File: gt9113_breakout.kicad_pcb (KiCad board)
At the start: 4 copper layers, 34.8 x 36 mm, 53 parts, among them J1 Conn_01x04_Male, J2 CONN_10118194-0001LF_AMP, J3 Conn_01x04_Male, J4 Conn_01x07_Male, J5 Conn_01x01_Male, J7 504740-5100, J8 504740-5100, Q1 2N7002E, U1 mXT2952TD, U2 HT7533-1-SOT89, Y1 DNF/16MHz

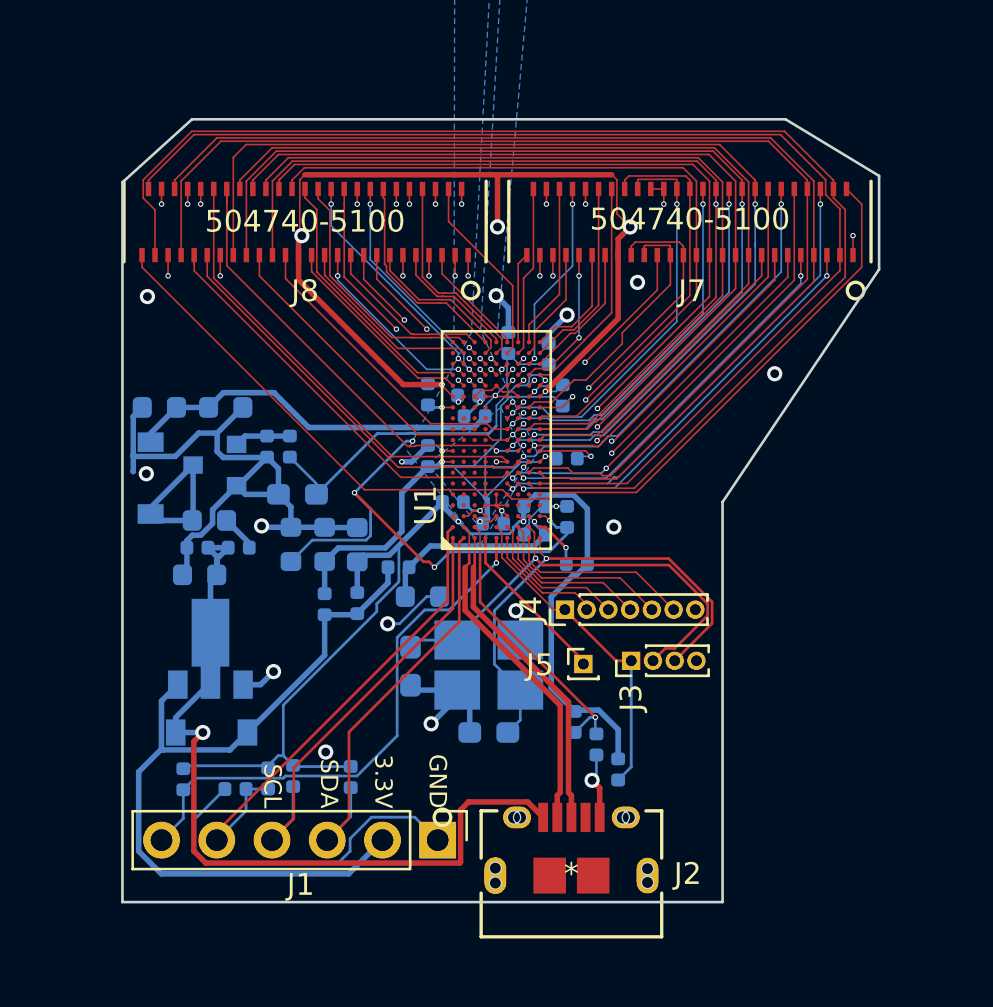
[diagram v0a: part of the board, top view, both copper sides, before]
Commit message: Remove all traces of atmxt2952. enable pth_and_npth_single_file since that's what jlcpcb wants
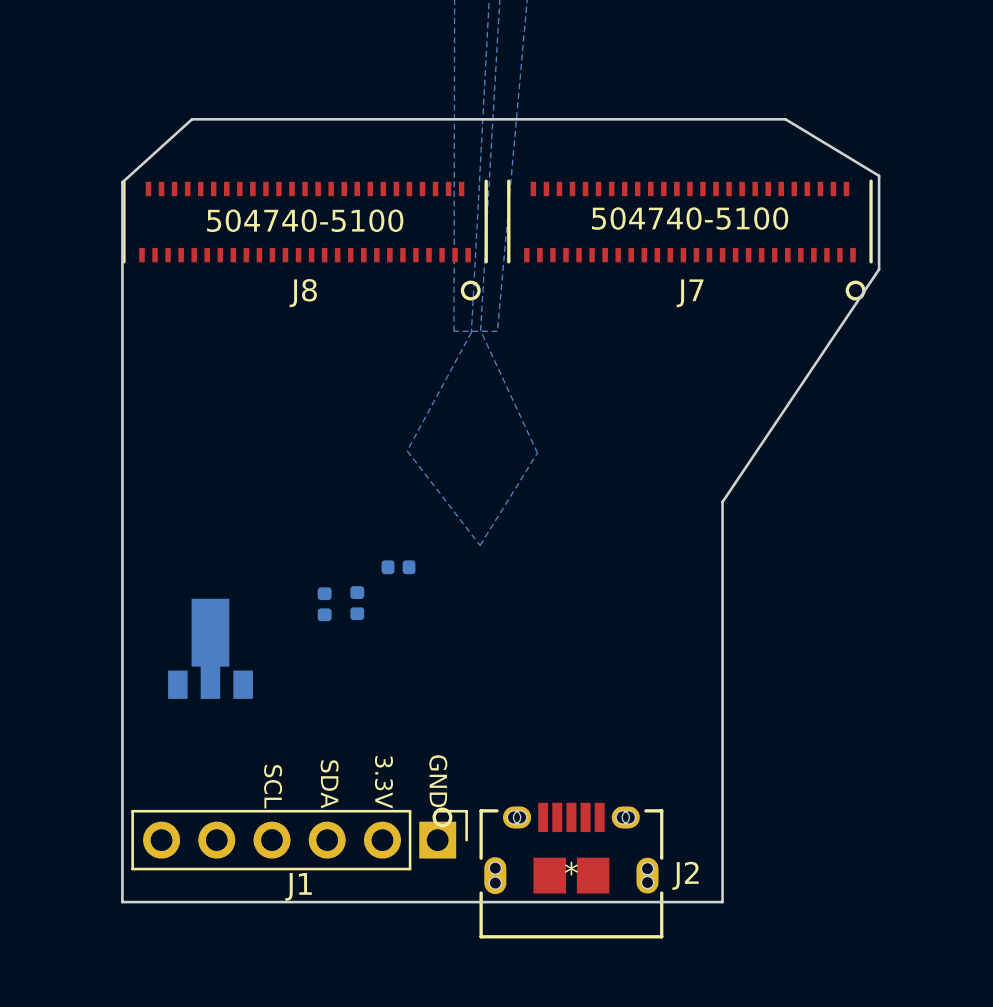
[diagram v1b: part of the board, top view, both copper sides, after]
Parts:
- removed C1, C11, C18, C20, C23, C7: 2.2uF, Capacitor_SMD:C_0603_1608Metric
- removed C10, C12, C13, C14, C16, C17, C19, C2, C21, C22, C25, C26, C8, C9: 22nF, Capacitor_SMD:C_0402_1005Metric
- removed C24, C27: DNF/15pF, Capacitor_SMD:C_0603_1608Metric_Pad1.05x0.95mm_HandSolder
- removed C3: DNF/33pF, Capacitor_SMD:C_0603_1608Metric_Pad1.05x0.95mm_HandSolder
- removed C4: 33pF, Capacitor_SMD:C_0402_1005Metric
- removed C5: 10nF, Capacitor_SMD:C_0402_1005Metric
- removed C6: 10uF, Capacitor_SMD:C_0603_1608Metric
- removed D1, D2: D_Schottky, Diode_SMD:D_SOD-123
- removed J3: Conn_01x04_Male, Connector_PinHeader_1.00mm:PinHeader_1x04_P1.00mm_Vertical
- removed J4: Conn_01x07_Male, Connector_PinHeader_1.00mm:PinHeader_1x07_P1.00mm_Vertical
- removed J5: Conn_01x01_Male, Connector_PinHeader_1.00mm:PinHeader_1x01_P1.00mm_Vertical
- removed L1: 10uH, Inductor_SMD:L_0603_1608Metric
- removed Q1: 2N7002E, Package_TO_SOT_SMD:SOT-23
- removed R1: 10, Resistor_SMD:R_0402_1005Metric
- removed R13, R3, R4: 10k, Resistor_SMD:R_0402_1005Metric
- removed R2: 47, Resistor_SMD:R_0402_1005Metric
- removed R5: 47k, Resistor_SMD:R_0402_1005Metric
- removed R6, R7: 3.3k, Resistor_SMD:R_0402_1005Metric
- removed R8: 0, Resistor_SMD:R_0402_1005Metric
- removed R9: 100k, Resistor_SMD:R_0402_1005Metric
- removed U1: mXT2952TD, mXT2952TD:mXT2952TD
- removed Y1: DNF/16MHz, Crystal:Crystal_SMD_3225-4Pin_3.2x2.5mm_HandSoldering
- J2: value CONN_10118194-0001LF_AMP -> 10118194-0001LF
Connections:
- net /VBUS renamed /VIN_5.0
- J1 pad 3: /SDA -> (no net)
- J1 pad 4: /SCL -> (no net)
- J1 pad 5: /~RESET -> (no net)
- J1 pad 6: /~CHG -> (no net)
- J2 pad 2: /USBD- -> (no net)
- J2 pad 3: /USBD+ -> (no net)
- J2 pad 4: Net-(J2-Pad4) -> (no net)
- J7 pad 31: /Y29 -> (no net)
- J7 pad 38: /X0 -> (no net)
- J7 pad 39: /X1 -> (no net)
- J7 pad 40: /X2 -> (no net)
- J7 pad 41: /X3 -> (no net)
- J7 pad 42: /X4 -> (no net)
- J7 pad 43: /X5 -> (no net)
- J7 pad 44: /X6 -> (no net)
- J7 pad 45: /X7 -> (no net)
- J7 pad 46: /X8 -> (no net)
- J7 pad 47: /X9 -> (no net)
- J7 pad 48: /X10 -> (no net)
- J7 pad 49: /X11 -> (no net)
- J7 pad 50: /X12 -> (no net)
- J7 pad 51: /X13 -> (no net)
- J8 pad 1: /X14 -> (no net)
- J8 pad 10: /X23 -> (no net)
- J8 pad 11: /X24 -> (no net)
- J8 pad 12: /X25 -> (no net)
- J8 pad 13: /X26 -> (no net)
- J8 pad 14: /X27 -> (no net)
- J8 pad 15: /X28 -> (no net)
- J8 pad 16: /X29 -> (no net)
- J8 pad 17: /X30 -> (no net)
- J8 pad 18: /X31 -> (no net)
- J8 pad 19: /X32 -> (no net)
- J8 pad 2: /X15 -> (no net)
- J8 pad 20: /X33 -> (no net)
- J8 pad 21: /X34 -> (no net)
- J8 pad 22: /X35 -> (no net)
- J8 pad 23: /X36 -> (no net)
- J8 pad 24: /X37 -> (no net)
- J8 pad 25: /X38 -> (no net)
- J8 pad 26: /X39 -> (no net)
- J8 pad 3: /X16 -> (no net)
- J8 pad 4: /X17 -> (no net)
- J8 pad 5: /X18 -> (no net)
- J8 pad 6: /X19 -> (no net)
- J8 pad 7: /X20 -> (no net)
- J8 pad 8: /X21 -> (no net)
- J8 pad 9: /X22 -> (no net)
- R11 pad 1: /VDDIO -> (no net)
- R12 pad 1: /VDD -> (no net)
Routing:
- net GND: track 132.0 -> 0.00 mm, vias 27 -> 0
- net /Y2: track 60.6 -> 0.00 mm
- net /Y1: track 55.6 -> 0.00 mm
- net /Y6: track 55.0 -> 0.00 mm
- net /Y5: track 52.5 -> 0.00 mm
- net /VDDIO: track 50.6 -> 0.00 mm, vias 2 -> 0
- net /Y14: track 49.1 -> 0.00 mm, vias 2 -> 0
- net /Y0: track 46.4 -> 0.00 mm
- net /Y16: track 45.1 -> 0.00 mm, vias 2 -> 0
- net /AVDD: track 44.8 -> 0.00 mm, vias 5 -> 0
- net /Y3: track 44.3 -> 0.00 mm, vias 3 -> 0
- net /Y4: track 43.5 -> 0.00 mm, vias 3 -> 0
- net /Y15: track 42.5 -> 0.00 mm
- net /Y17: track 41.4 -> 0.00 mm, vias 2 -> 0
- net /Y7: track 41.2 -> 0.00 mm, vias 3 -> 0
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- removed copper zone on B.Cu, net /AVDD
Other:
- net class BGA removed
- net class Default: clearance 0.0762 -> 0.127; trace_width 0.0762 -> 0.127; via_dia 0.25 -> 0.45; via_drill 0.15 -> 0.2
- rule trace_clearance: 0.0762 -> 0.127
- rule trace_min: 0.076 -> 0.127
- rule via_min_drill: 0.15 -> 0.2
- rule via_min_size: 0.25 -> 0.45

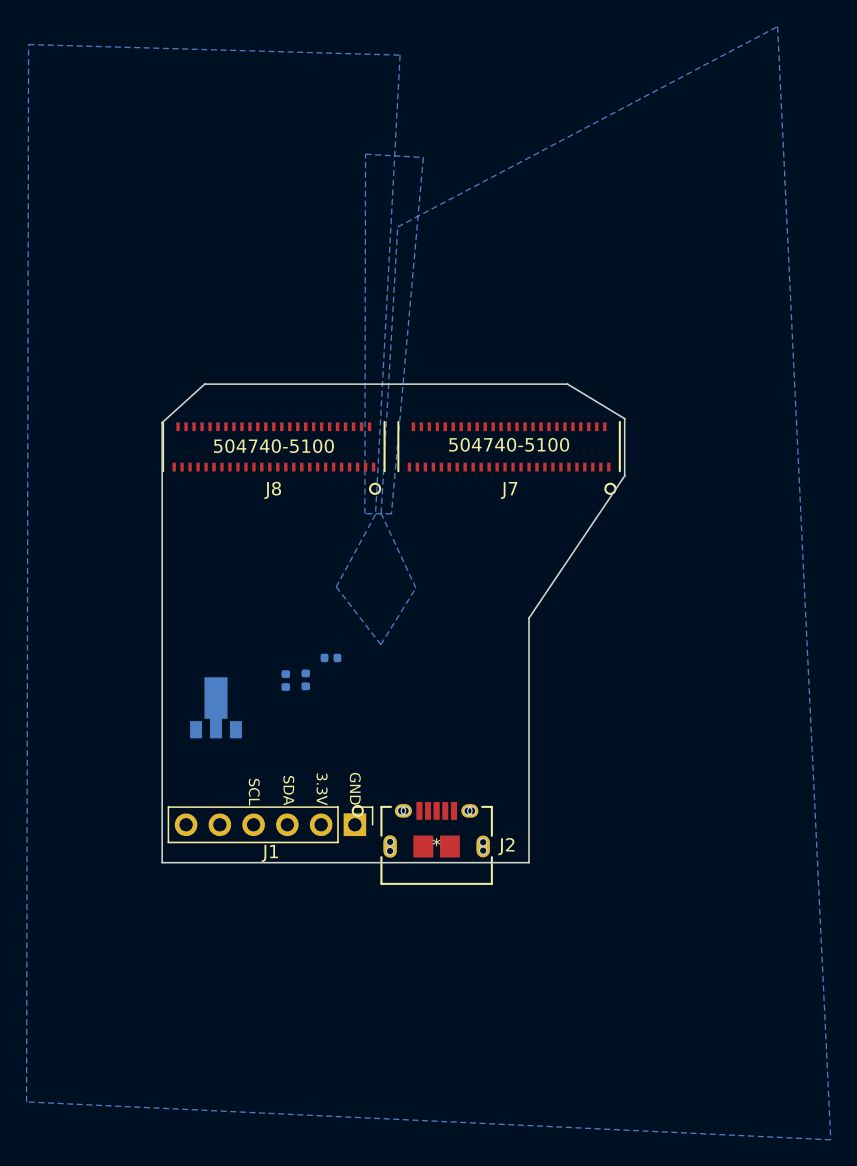
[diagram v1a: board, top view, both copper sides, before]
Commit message: Add footprint for GT9113. Start to route the drive/sense pins.
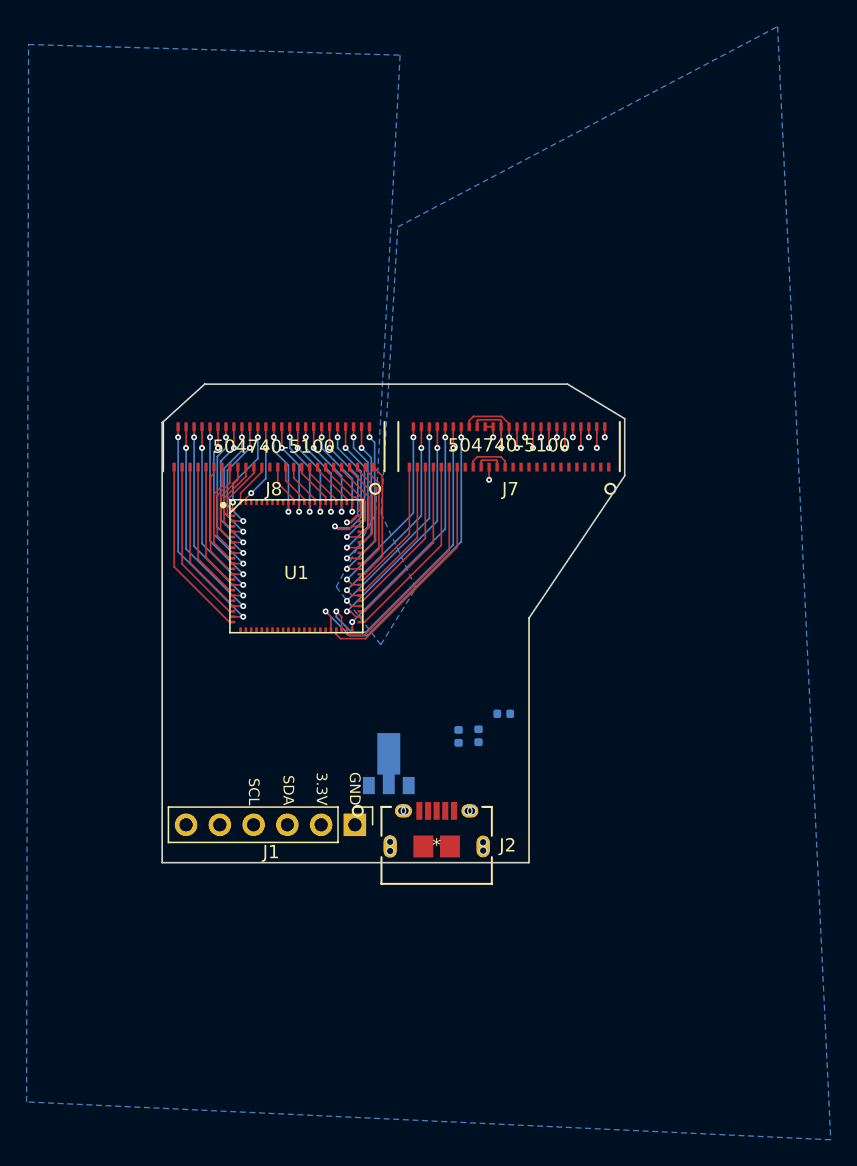
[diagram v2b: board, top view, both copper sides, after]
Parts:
- added U1: GT9113, footprints:GT9113, F.Cu at (138.9, 83.7)
- moved R10 13.7 mm to (151.1, 96.5)
- moved R11 13.7 mm to (152.6, 96.5)
- moved R12 13.7 mm to (154.5, 94.8)
- moved U2 13.7 mm to (145.8, 98.5)
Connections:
- J7 pad 31: (no net) -> /Y29
- J7 pad 38: (no net) -> /X0
- J7 pad 39: (no net) -> /X1
- J7 pad 40: (no net) -> /X2
- J7 pad 41: (no net) -> /X3
- J7 pad 42: (no net) -> /X4
- J7 pad 43: (no net) -> /X5
- J7 pad 44: (no net) -> /X6
- J7 pad 45: (no net) -> /X7
- J7 pad 46: (no net) -> /X8
- J7 pad 47: (no net) -> /X9
- J7 pad 48: (no net) -> /X10
- J7 pad 49: (no net) -> /X11
- J7 pad 50: (no net) -> /X12
- J7 pad 51: (no net) -> /X13
- J8 pad 1: (no net) -> /X14
- J8 pad 10: (no net) -> /X23
- J8 pad 11: (no net) -> /X24
- J8 pad 12: (no net) -> /X25
- J8 pad 13: (no net) -> /X26
- J8 pad 14: (no net) -> /X27
- J8 pad 15: (no net) -> /X28
- J8 pad 16: (no net) -> /X29
- J8 pad 17: (no net) -> /X30
- J8 pad 18: (no net) -> /X31
- J8 pad 19: (no net) -> /X32
- J8 pad 2: (no net) -> /X15
- J8 pad 20: (no net) -> /X33
- J8 pad 21: (no net) -> /X34
- J8 pad 22: (no net) -> /X35
- J8 pad 23: (no net) -> /X36
- J8 pad 24: (no net) -> /X37
- J8 pad 25: (no net) -> /X38
- J8 pad 26: (no net) -> /X39
- J8 pad 3: (no net) -> /X16
- J8 pad 4: (no net) -> /X17
- J8 pad 5: (no net) -> /X18
- J8 pad 6: (no net) -> /X19
- J8 pad 7: (no net) -> /X20
- J8 pad 8: (no net) -> /X21
- J8 pad 9: (no net) -> /X22
- R10 pad 1: /AVDD -> (no net)
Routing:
- net /X0: track 0.00 -> 24.1 mm, vias 0 -> 2
- net /X2: track 0.00 -> 22.9 mm, vias 0 -> 2
- net /X1: track 0.00 -> 18.4 mm
- net /X4: track 0.00 -> 18.2 mm, vias 0 -> 2
- net /X6: track 0.00 -> 17.9 mm, vias 0 -> 2
- net /Y1: track 0.00 -> 17.1 mm, vias 0 -> 2
- net /X3: track 0.00 -> 17.0 mm
- net /X8: track 0.00 -> 16.8 mm, vias 0 -> 2
- net /Y3: track 0.00 -> 16.1 mm, vias 0 -> 2
- net /X10: track 0.00 -> 15.8 mm, vias 0 -> 2
- net /Y5: track 0.00 -> 15.0 mm, vias 0 -> 2
- net /X12: track 0.00 -> 14.7 mm, vias 0 -> 2
- net /Y0: track 0.00 -> 14.4 mm, vias 0 -> 1
- net /X5: track 0.00 -> 14.4 mm
- net /Y2: track 0.00 -> 14.2 mm, vias 0 -> 1
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
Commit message: Fix up USB connector footprint so I don't have to ignore DRC errors. Add courtyard for gt9113 footprint. Wire up digital IO pins to 2.54mm header. Tweak X/Y traces.
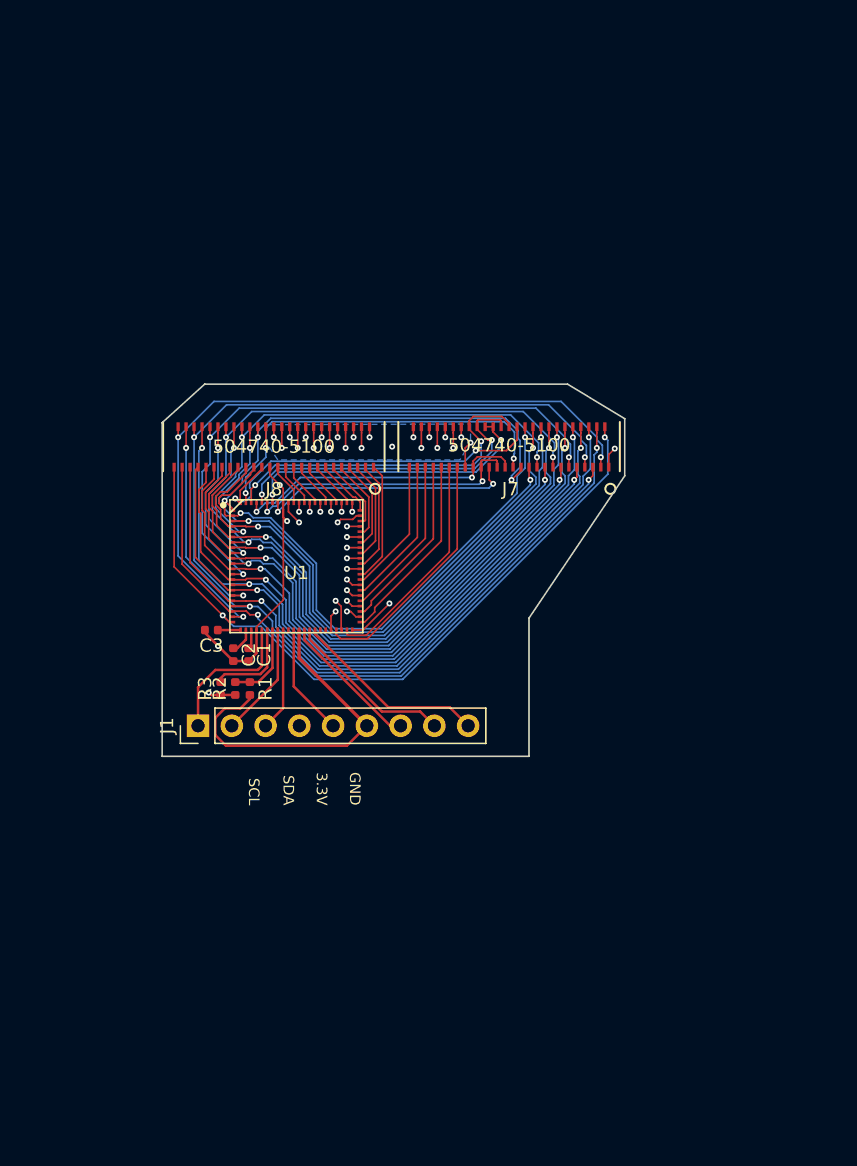
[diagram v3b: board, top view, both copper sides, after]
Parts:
- removed J2: 10118194-0001LF, usb port:10118194-0001LF
- removed R10, R11, R12: 0, Resistor_SMD:R_0402_1005Metric
- removed U2: HT7533-1-SOT89, Package_TO_SOT_SMD:SOT-89-3
- added C1: 2.2uF, Capacitor_SMD:C_0402_1005Metric, F.Cu at (135.3, 90.3)
- added C2: 2.2uF, Capacitor_SMD:C_0402_1005Metric, F.Cu at (134.2, 90.3)
- added C3: 2.2uF, Capacitor_SMD:C_0402_1005Metric, F.Cu at (132.5, 88.5)
- added R1: 0R/DNF, Resistor_SMD:R_0402_1005Metric, F.Cu at (135.4, 92.9)
- added R2: 0R/DNF, Resistor_SMD:R_0402_1005Metric, F.Cu at (134.3, 92.9)
- added R3: 300k/DNF, Resistor_SMD:R_0402_1005Metric, F.Cu at (133.2, 92.9)
- J1: value Conn_01x04_Male -> Conn_01x09_Male; footprint Connector_PinHeader_2.54mm:PinHeader_1x06_P2.54mm_Vertical -> Connector_PinHeader_2.54mm:PinHeader_1x09_P2.54mm_Vertical
- moved J1 14.0 mm to (131.5, 95.7), turned to 90 degrees
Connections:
- J1 pad 1: GND -> /CLK_ADJ
- J1 pad 2: /VIN_3.3 -> /SDA
- J1 pad 3: (no net) -> /SCL
- J1 pad 4: (no net) -> GND
- J1 pad 5: (no net) -> /SYNC
- J1 pad 6: (no net) -> /VIN_3.3
- U1 pad 23: (no net) -> Net-(C3-Pad1)
- U1 pad 24: (no net) -> Net-(C2-Pad1)
- U1 pad 25: (no net) -> Net-(C1-Pad1)
- U1 pad 26: (no net) -> GND
- U1 pad 27: (no net) -> /CLK_ADJ
- U1 pad 28: (no net) -> Net-(R3-Pad2)
- U1 pad 29: (no net) -> Net-(R1-Pad1)
- U1 pad 30: (no net) -> /SDA
- U1 pad 31: (no net) -> /SCL
- U1 pad 32: (no net) -> Net-(U1-Pad32)
- U1 pad 33: (no net) -> /SYNC
- U1 pad 34: (no net) -> /VIN_3.3
- U1 pad 35: (no net) -> /ARM_RST
- U1 pad 36: (no net) -> /Wake
- U1 pad 37: (no net) -> /RSTB
- U1 pad 38: (no net) -> Net-(U1-Pad38)
- U1 pad 39: (no net) -> Net-(U1-Pad39)
- U1 pad 80: (no net) -> GND
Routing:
- net /Y0: track 14.4 -> 54.7 mm, vias 1 -> 2
- net /Y4: track 12.4 -> 51.0 mm, vias 1 -> 2
- net /Y8: track 10.3 -> 48.8 mm, vias 1 -> 2
- net /Y2: track 14.2 -> 52.3 mm, vias 1 -> 2
- net /Y12: track 8.63 -> 46.7 mm, vias 1 -> 2
- net /Y6: track 12.1 -> 50.1 mm, vias 1 -> 2
- net /Y10: track 10.2 -> 48.0 mm, vias 1 -> 2
- net /Y14: track 8.67 -> 46.0 mm, vias 1 -> 2
- net /Y16: track 7.16 -> 44.3 mm, vias 1 -> 2
- net /Y18: track 7.19 -> 44.1 mm, vias 1 -> 2
- net /Y20: track 5.63 -> 42.4 mm, vias 1 -> 2
- net /Y7: track 14.0 -> 50.6 mm, vias 2 -> 3
- net /Y3: track 16.1 -> 52.6 mm, vias 2 -> 3
- net /Y1: track 17.1 -> 53.5 mm, vias 2 -> 3
- net /Y11: track 12.1 -> 48.0 mm, vias 2 -> 3
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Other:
- board size 34.8 x 36 mm -> 34.8 x 28 mm

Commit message: Convert to Kicad 5.99 format
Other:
- net class Default removed
- net class Power removed
